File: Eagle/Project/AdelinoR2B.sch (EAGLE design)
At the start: 70 parts, among them J1 DC-044-A, J2 YELLOW-8P-2.54, J3 YELLOW-6P-2.54, J4 YELLOW-8P-2.54, J5 YELLOW-8P-2.54, J6 4P-2.0, J7 YELLOW-2X3P-2.54, J8 4P-2.0, Q1 NCE3407A, Q2 CJ2305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

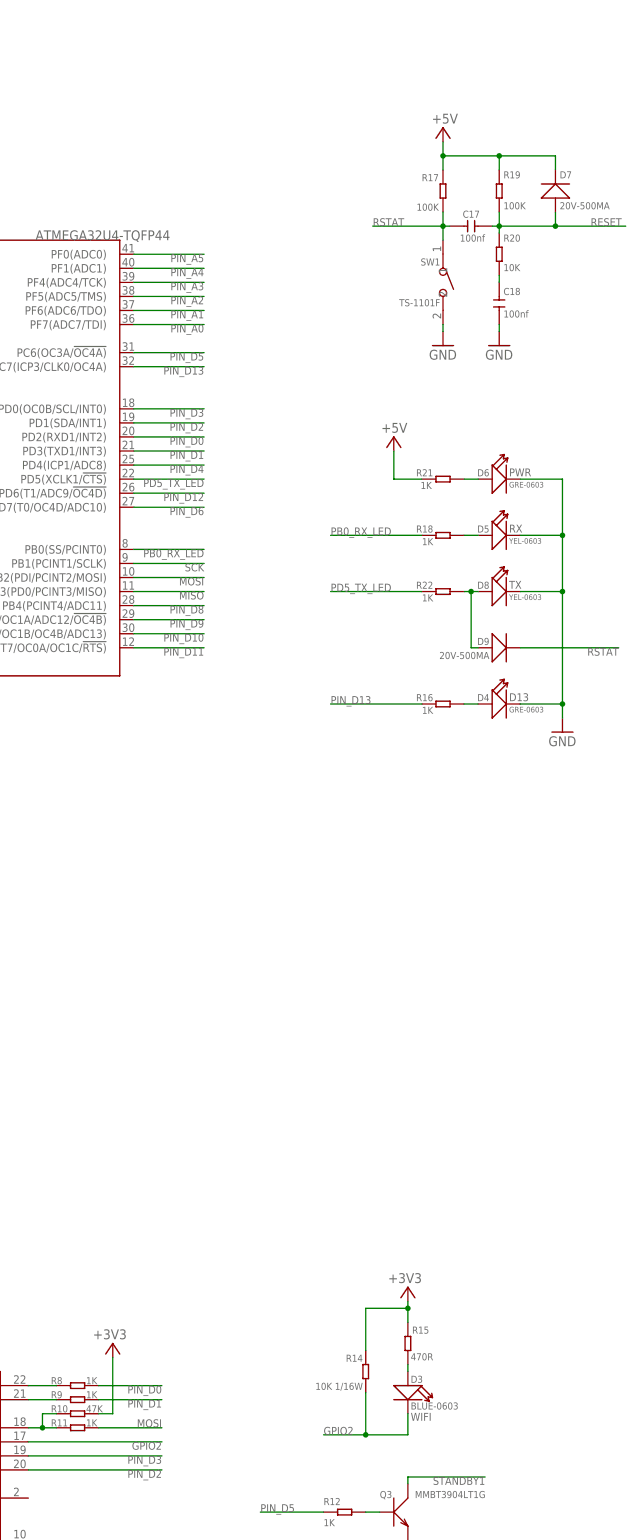
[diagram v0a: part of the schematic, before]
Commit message: Update GPIO0 wires.
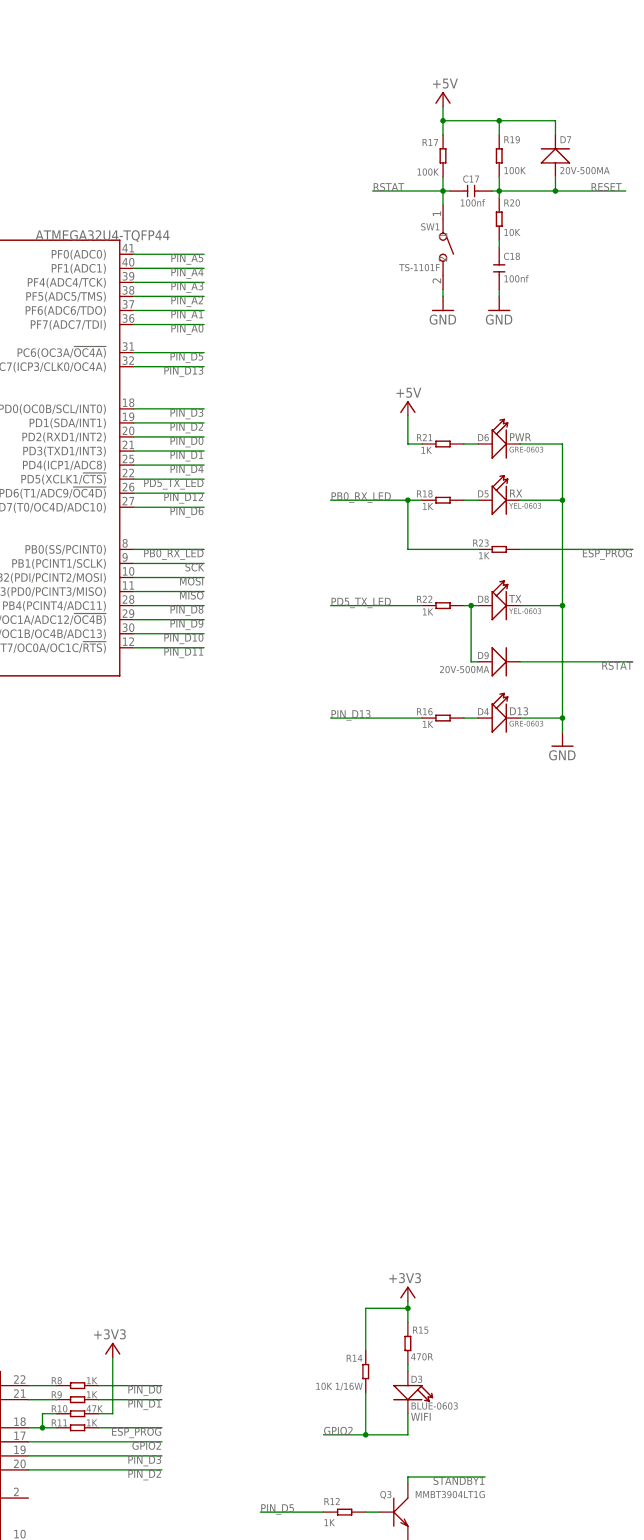
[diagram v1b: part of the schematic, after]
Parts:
- added R23: 1K, Seeed-Resistor:SMD-RES-1K-5%-1/16W(0402)
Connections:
- new net ESP_PROG: R11.2, R23.2
- net MOSI: no longer R11.2
- net PB0_RX_LED: now also R23.1
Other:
- moved on the sheet: C17, C18, D4, D5, D6, D7, D8, D9, R16, R17, R18, R19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

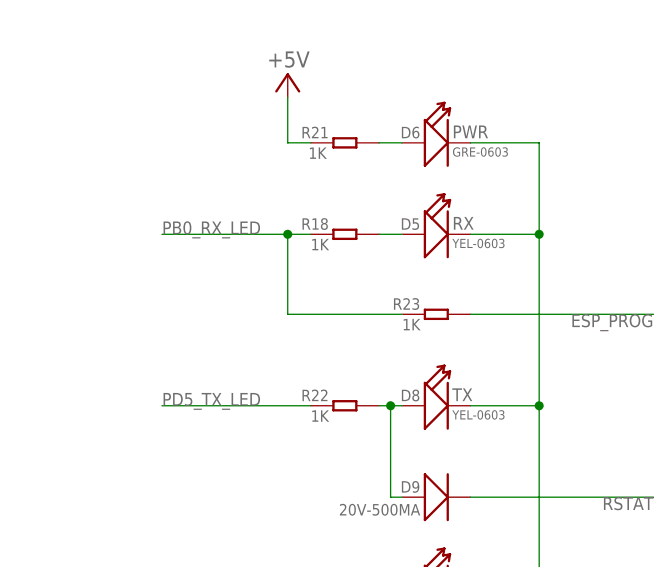
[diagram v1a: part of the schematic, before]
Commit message: Remove redundant resistor from GPIO0 wiring.
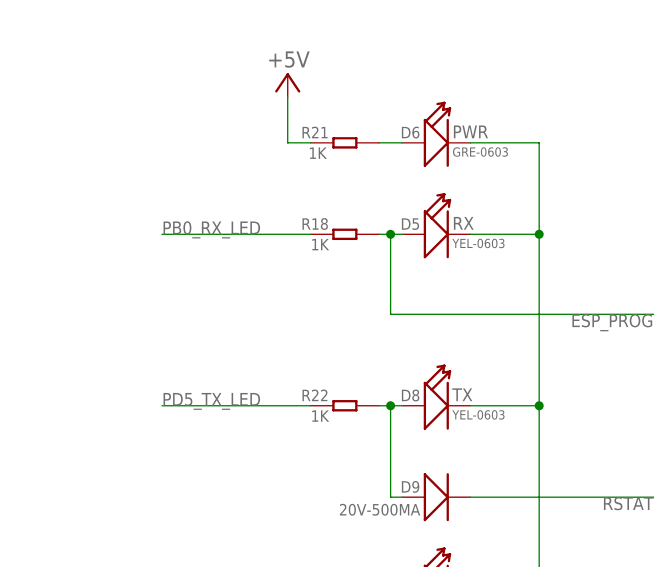
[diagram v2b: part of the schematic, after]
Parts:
- removed R23: 1K, Seeed-Resistor:SMD-RES-1K-5%-1/16W(0402)
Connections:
- removed net N$6: D5.+, R18.2
- net ESP_PROG: now also D5.+, R18.2; no longer R23.2
- net PB0_RX_LED: no longer R23.1
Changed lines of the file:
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@@
 <part name="R22" library="Seeed-Resistor" deviceset="SMD-RES-1K-5%-1/16W(0402)" device="" value="1K"/>
 <part name="D9" library="Seeed-Diode" deviceset="SMD-DIODE-SCHOTTKY-20V-500MA(SOD-123)P" device="" value="20V-500MA"/>
-<part name="R23" library="Seeed-Resistor" deviceset="SMD-RES-1K-5%-1/16W(0402)" device="" value="1K"/>
 </parts>
 <sheets>
@@
 <attribute name="NAME" x="212.852" y="61.468" size="1.27" layer="95" ratio="10" rot="R180"/>
 <attribute name="VALUE" x="212.852" y="58.928" size="1.27" layer="96" ratio="10" rot="R180"/>
-</instance>
-<instance part="R23" gate="G$1" x="214.63" y="80.01" smashed="yes">
-<attribute name="NAME" x="212.852" y="81.788" size="1.27" layer="95" ratio="10" rot="R180"/>
-<attribute name="VALUE" x="212.852" y="79.502" size="1.27" layer="96" ratio="10" rot="R180"/>
 </instance>
 </instances>
@@
 </segment>
 </net>
-<net name="N$6" class="0">
-<segment>
-<pinref part="R18" gate="G$1" pin="2"/>
-<pinref part="D5" gate="G$1" pin="+"/>
-<wire x1="208.28" y1="88.9" x2="210.82" y2="88.9" width="0.1524" layer="91"/>
-</segment>
-</net>
 <net name="N$8" class="0">
 <segment>
@@
 <segment>
 <pinref part="R18" gate="G$1" pin="1"/>
-<wire x1="200.66" y1="88.9" x2="198.12" y2="88.9" width="0.1524" layer="91"/>
 <label x="184.15" y="88.9" size="1.4224" layer="95"/>
-<pinref part="R23" gate="G$1" pin="1"/>
-<wire x1="198.12" y1="88.9" x2="184.15" y2="88.9" width="0.1524" layer="91"/>
-<wire x1="210.82" y1="80.01" x2="198.12" y2="80.01" width="0.1524" layer="91"/>
-<wire x1="198.12" y1="80.01" x2="198.12" y2="88.9" width="0.1524" layer="91"/>
-<junction x="198.12" y="88.9"/>
+<wire x1="200.66" y1="88.9" x2="184.15" y2="88.9" width="0.1524" layer="91"/>
 </segment>
 </net>
@@
 <net name="ESP_PROG" class="0">
 <segment>
-<pinref part="R23" gate="G$1" pin="2"/>
-<wire x1="218.44" y1="80.01" x2="238.76" y2="80.01" width="0.1524" layer="91"/>
+<wire x1="209.55" y1="80.01" x2="238.76" y2="80.01" width="0.1524" layer="91"/>
 <label x="238.76" y="80.01" size="1.4224" layer="95" rot="R180"/>
-</segment>
-<segment>
+<pinref part="R18" gate="G$1" pin="2"/>
+<pinref part="D5" gate="G$1" pin="+"/>
+<wire x1="208.28" y1="88.9" x2="209.55" y2="88.9" width="0.1524" layer="91"/>
+<wire x1="209.55" y1="88.9" x2="210.82" y2="88.9" width="0.1524" layer="91"/>
+<wire x1="209.55" y1="80.01" x2="209.55" y2="88.9" width="0.1524" layer="91"/>
+<junction x="209.55" y="88.9"/>
+</segment>
+<segment>

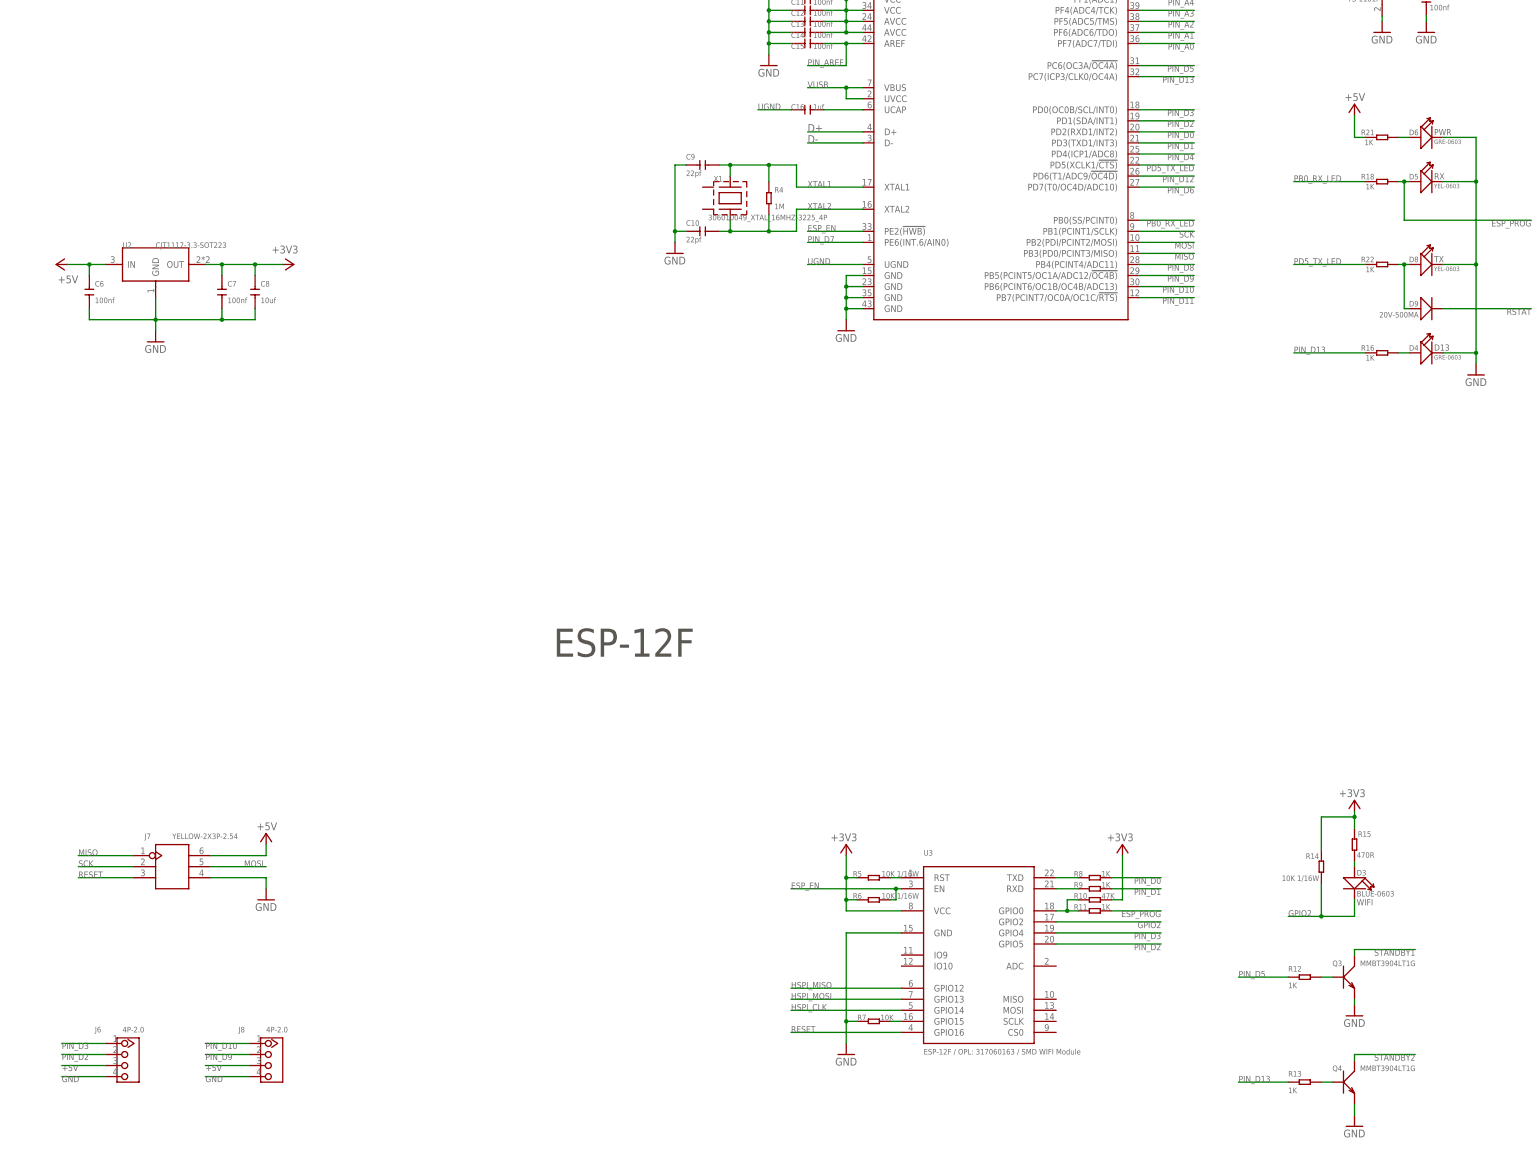
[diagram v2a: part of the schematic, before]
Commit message: Adding native SPI support.
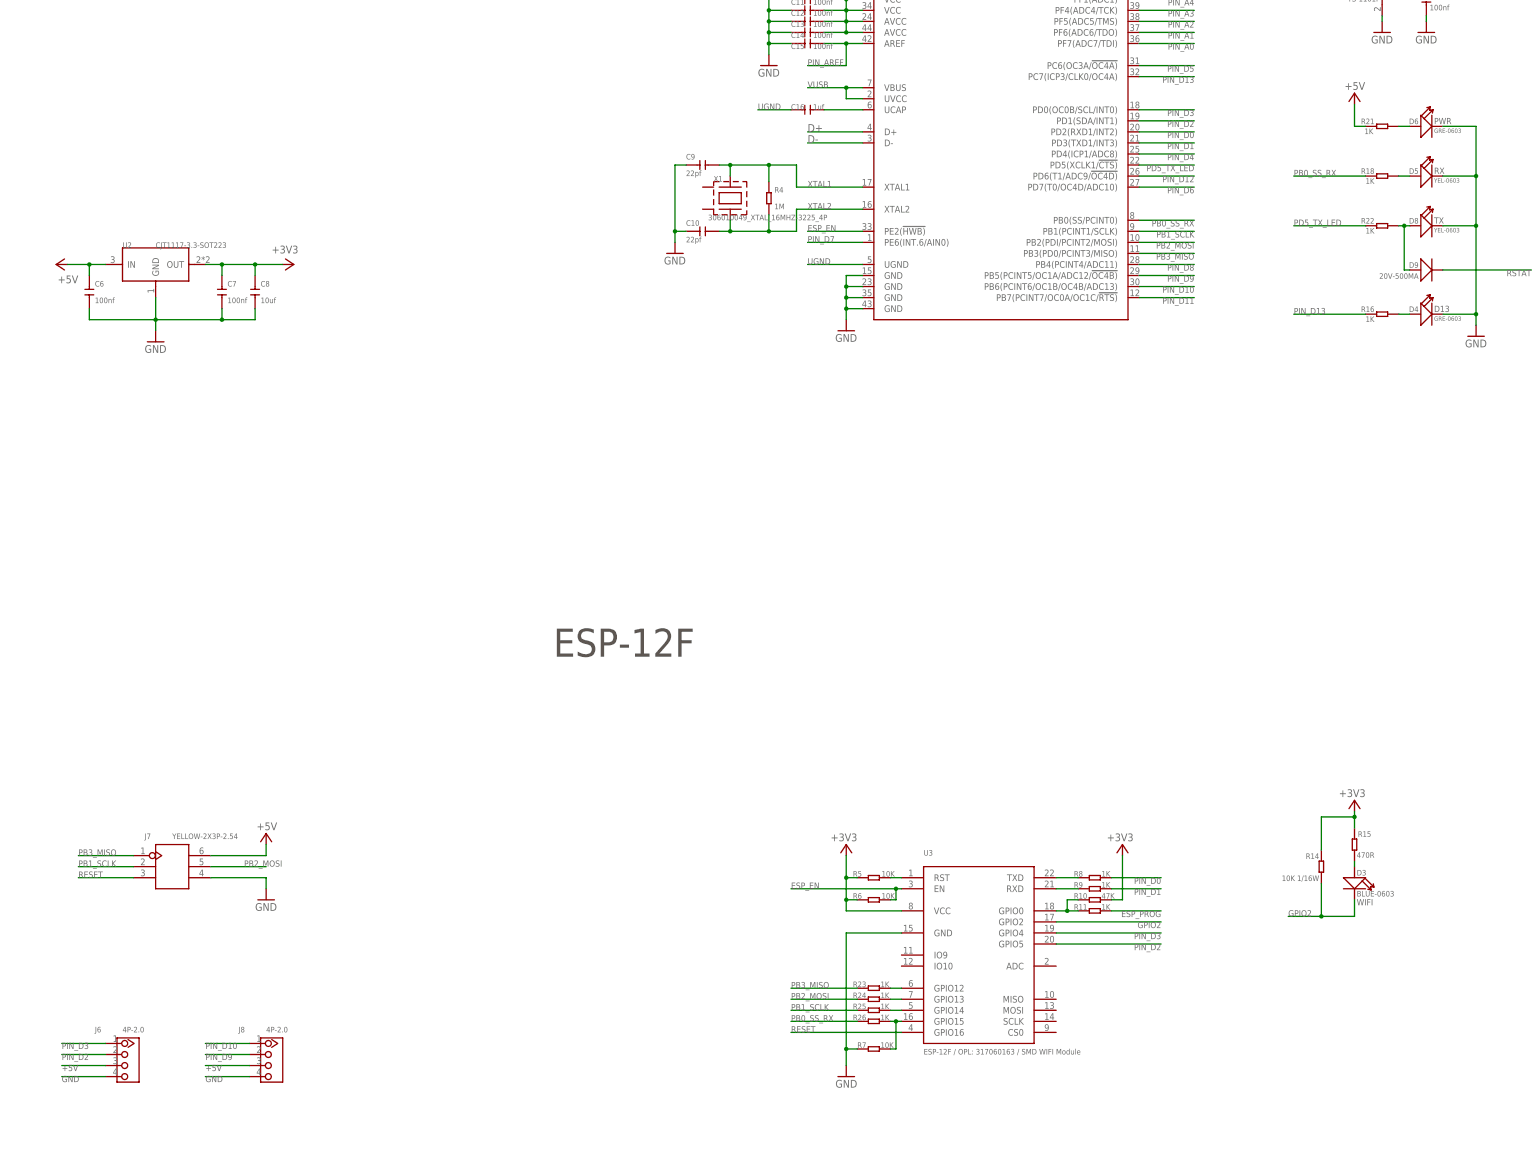
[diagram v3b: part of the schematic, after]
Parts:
- removed Q3, Q4: MMBT3904LT1G, Seeed-Transistor:SMD-TRANSISTORS-NPN-40V-200MA-MMBT3904LT1G(SOT-23)
- removed R12, R13: 1K, Seeed-Resistor:SMD-RES-1K-5%-1/16W(0402)
- added R23, R24, R25, R26: 1K, Seeed-Resistor:SMD-RES-1K-5%-1/16W(0402)
- R5, R6: value 10K 1/16W -> 10K
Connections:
- removed net HSPI_CLK: U3.GPIO14
- removed net HSPI_MISO: U3.GPIO12
- removed net HSPI_MOSI: U3.GPIO13
- removed net MISO: J7.1, U4.PB3(PD0/PCINT3/MISO)
- removed net MOSI: J7.5, U4.PB2(PDI/PCINT2/MOSI)
- removed net N$16: Q3.B, R12.2
- removed net N$21: Q4.B, R13.2
- removed net N$4: R7.2, U3.GPIO15
- removed net PB0_RX_LED: R18.1, U4.PB0(SS/PCINT0)
- removed net SCK: J7.2, U4.PB1(PCINT1/SCLK)
- removed net STANDBY1: Q3.C
- removed net STANDBY2: Q4.C
- new net N$15: D5.+, R18.2
- new net N$19: R24.2, U3.GPIO13
- new net N$20: R25.2, U3.GPIO14
- new net N$22: R26.2, R7.2, U3.GPIO15
- new net N$6: R23.2, U3.GPIO12
- new net PB0_SS_RX: R18.1, R26.1, U4.PB0(SS/PCINT0)
- new net PB1_SCLK: J7.2, R25.1, U4.PB1(PCINT1/SCLK)
- new net PB2_MOSI: J7.5, R24.1, U4.PB2(PDI/PCINT2/MOSI)
- new net PB3_MISO: J7.1, R23.1, U4.PB3(PD0/PCINT3/MISO)
- net ESP_PROG: no longer D5.+, R18.2
- net GND: no longer Q3.E, Q4.E
- net PIN_D13: no longer R13.1
- net PIN_D5: no longer R12.1
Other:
- moved on the sheet: D4, D5, D6, D8, D9, R16, R18, R21, R22, R7
